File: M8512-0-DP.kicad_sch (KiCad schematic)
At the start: 1 part, among them J1 KL10_6-bay_backplane_connector

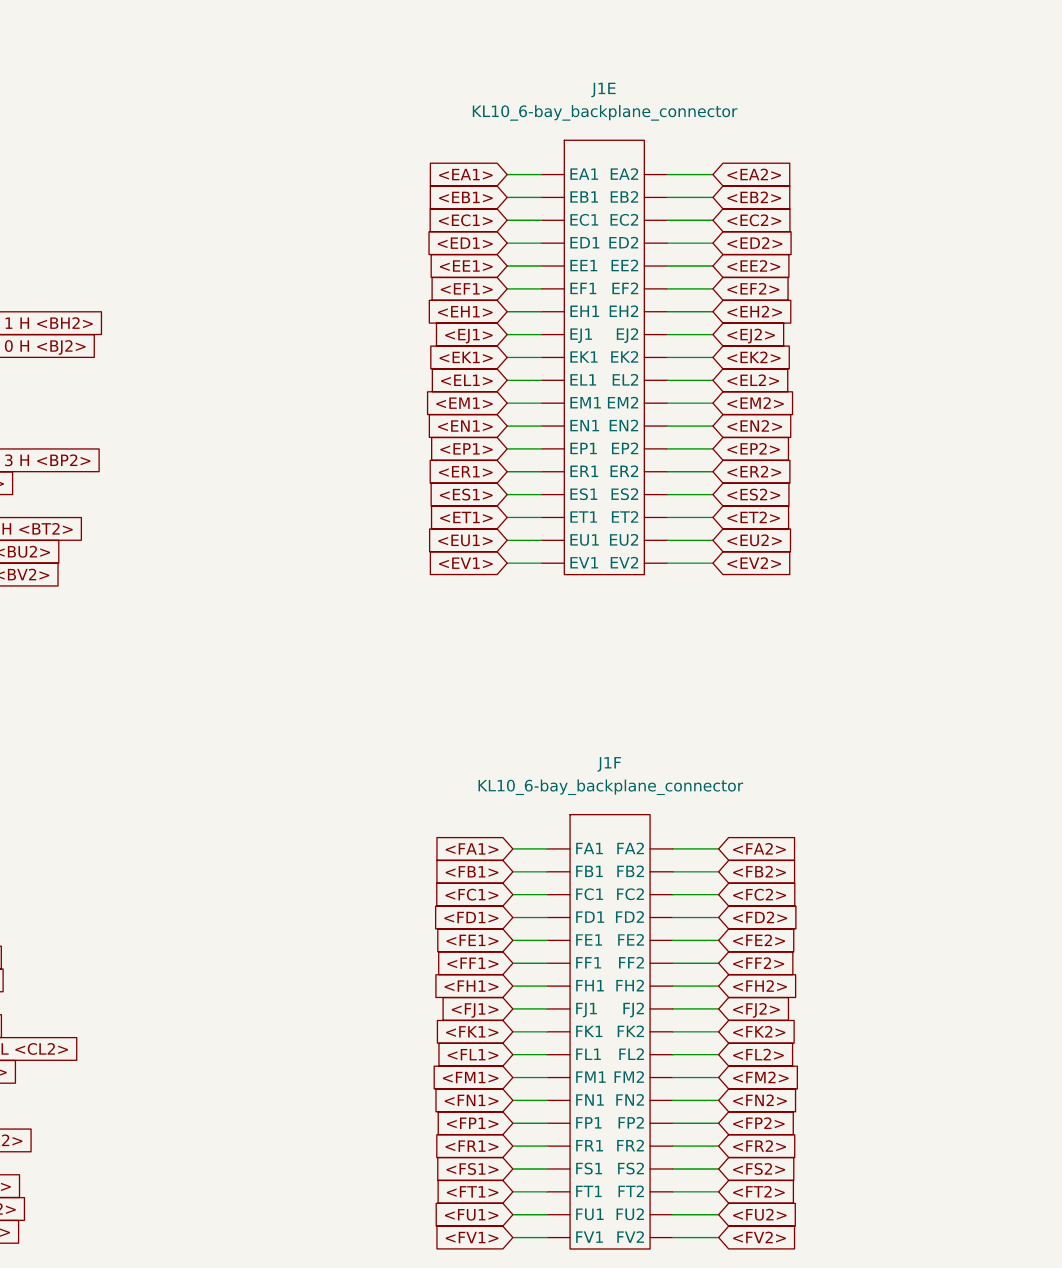
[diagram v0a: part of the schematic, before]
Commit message: Label BP connectors in EDP with their signal names.
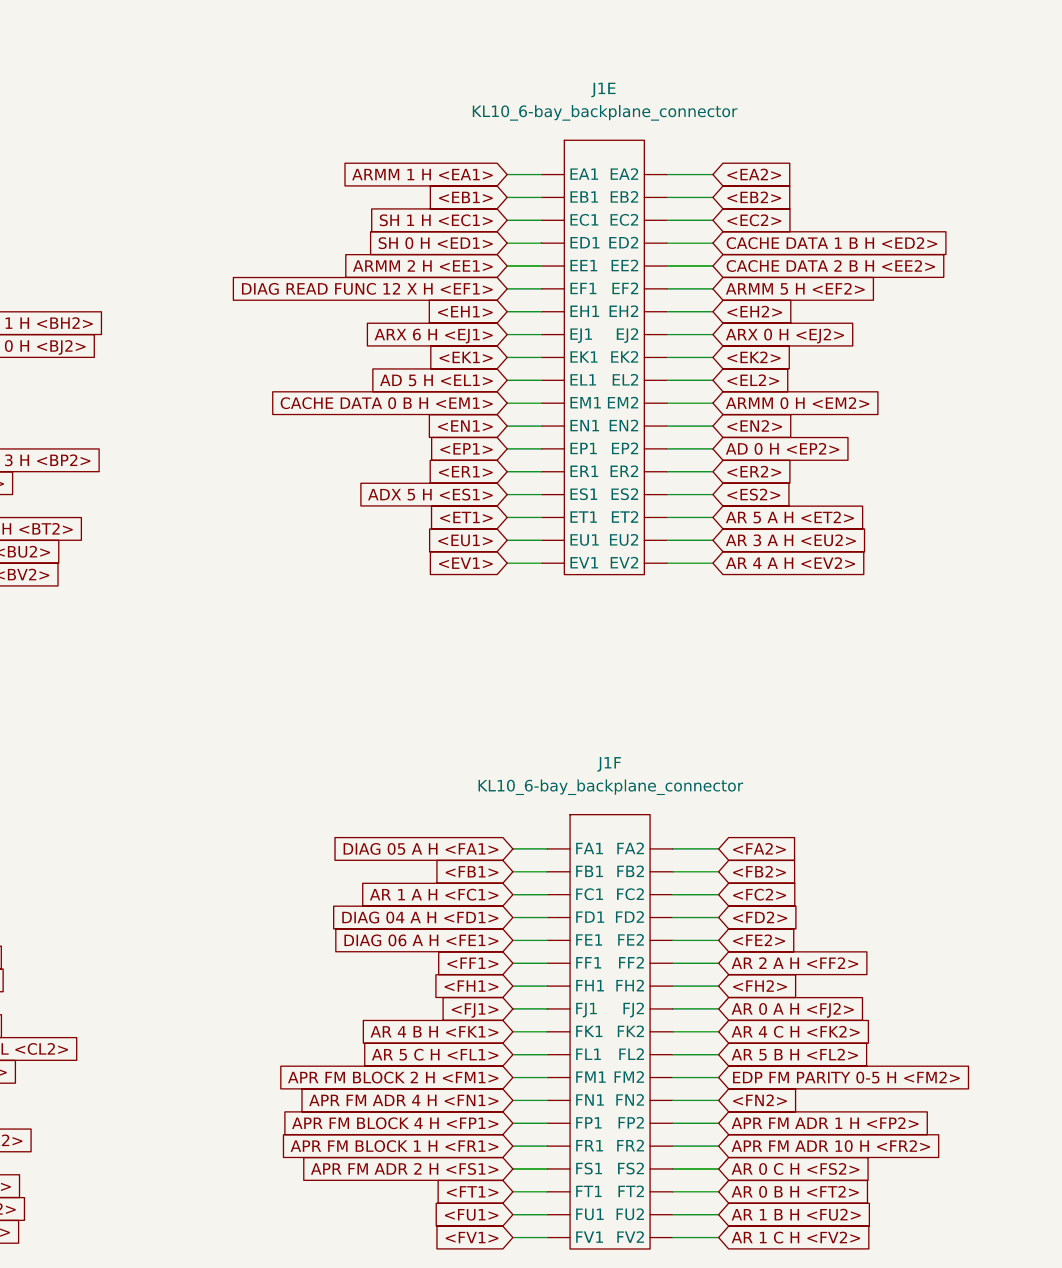
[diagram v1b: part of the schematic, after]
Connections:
- net <EA1> renamed ARMM 1 H <EA1>
- net <EC1> renamed SH 1 H <EC1>
- net <ED1> renamed SH 0 H <ED1>
- net <ED2> renamed CACHE DATA 1 B H <ED2>
- net <EE1> renamed ARMM 2 H <EE1>
- net <EE2> renamed CACHE DATA 2 B H <EE2>
- net <EF1> renamed DIAG READ FUNC 12 X H <EF1>
- net <EF2> renamed ARMM 5 H <EF2>
- net <EJ1> renamed ARX 6 H <EJ1>
- net <EJ2> renamed ARX 0 H <EJ2>
- net <EL1> renamed AD 5 H <EL1>
- net <EM1> renamed CACHE DATA 0 B H <EM1>
- net <EM2> renamed ARMM 0 H <EM2>
- net <EP2> renamed AD 0 H <EP2>
- net <ES1> renamed ADX 5 H <ES1>
- net <ET2> renamed AR 5 A H <ET2>
- net <EU2> renamed AR 3 A H <EU2>
- net <EV2> renamed AR 4 A H <EV2>
- net <FA1> renamed DIAG 05 A H <FA1>
- net <FC1> renamed AR 1 A H <FC1>
- net <FD1> renamed DIAG 04 A H <FD1>
- net <FE1> renamed DIAG 06 A H <FE1>
- net <FF2> renamed AR 2 A H <FF2>
- net <FJ2> renamed AR 0 A H <FJ2>
- net <FK1> renamed AR 4 B H <FK1>
- net <FK2> renamed AR 4 C H <FK2>
- net <FL1> renamed AR 5 C H <FL1>
- net <FL2> renamed AR 5 B H <FL2>
- net <FM1> renamed APR FM BLOCK 2 H <FM1>
- net <FM2> renamed EDP FM PARITY 0-5 H <FM2>
- net <FN1> renamed APR FM ADR 4 H <FN1>
- net <FP1> renamed APR FM BLOCK 4 H <FP1>
- net <FP2> renamed APR FM ADR 1 H <FP2>
- net <FR1> renamed APR FM BLOCK 1 H <FR1>
- net <FR2> renamed APR FM ADR 10 H <FR2>
- net <FS1> renamed APR FM ADR 2 H <FS1>
- net <FS2> renamed AR 0 C H <FS2>
- net <FT2> renamed AR 0 B H <FT2>
- net <FU2> renamed AR 1 B H <FU2>
- net <FV2> renamed AR 1 C H <FV2>

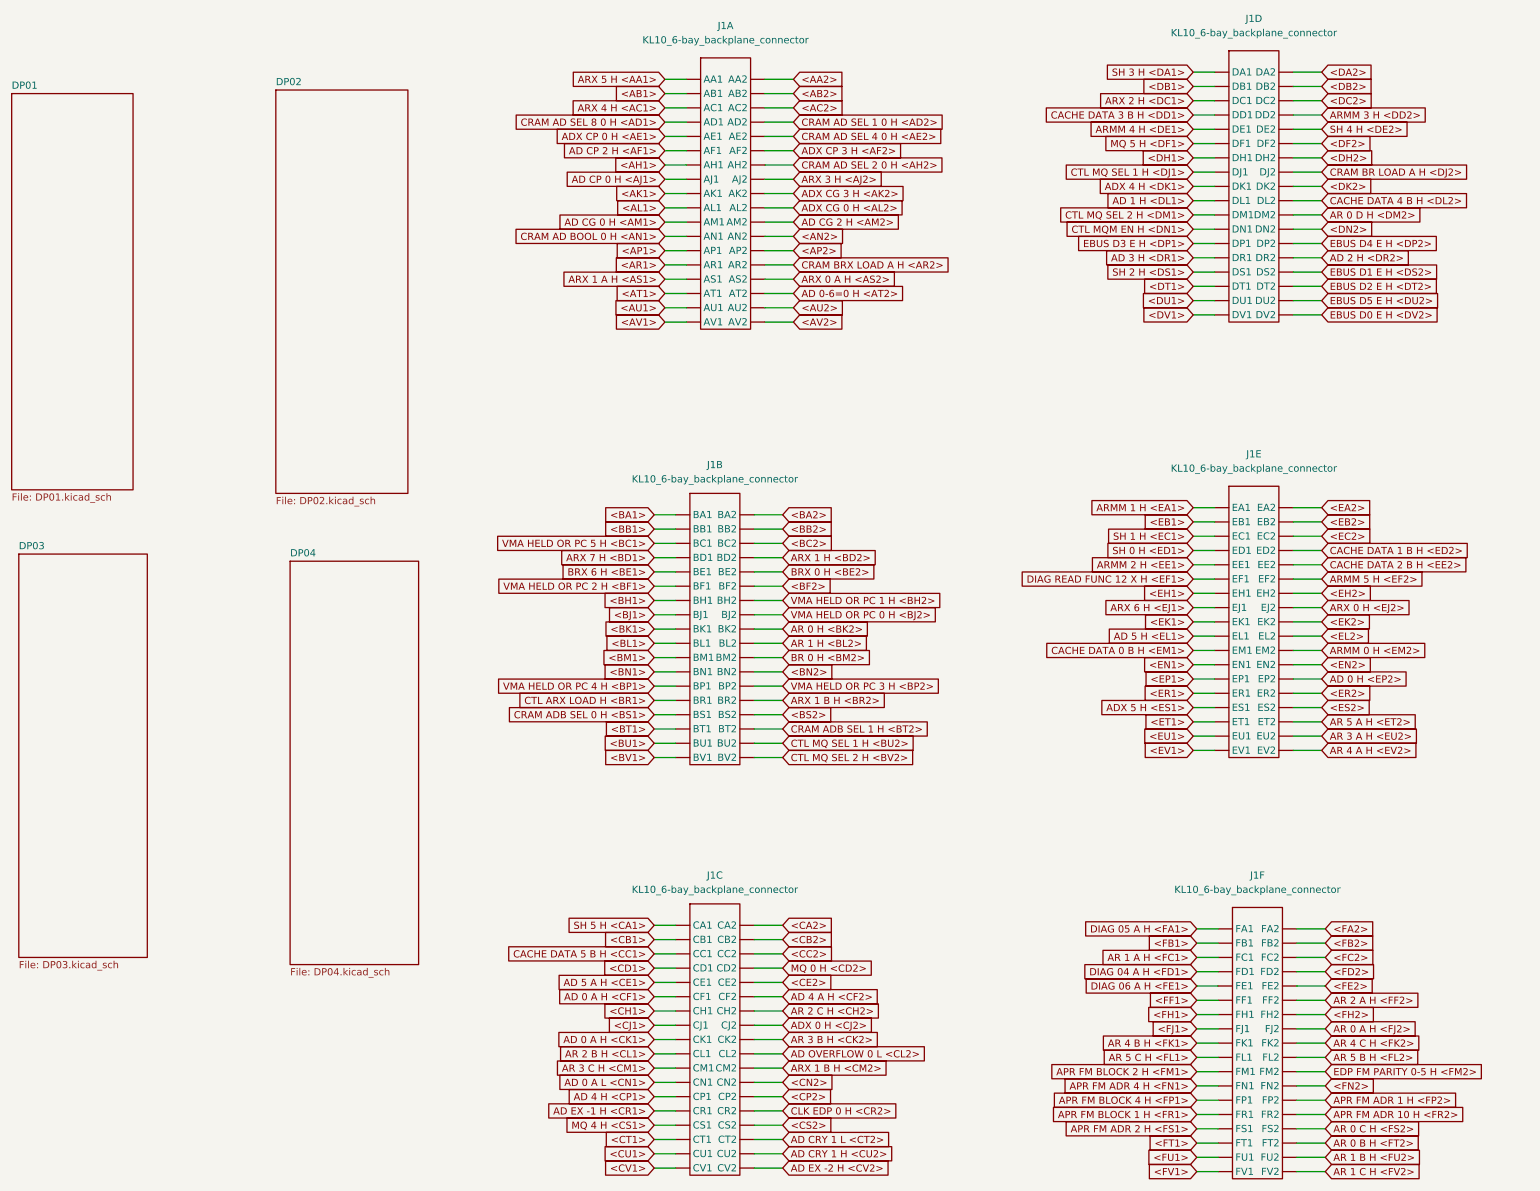
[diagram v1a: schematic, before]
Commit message: Wire up backplane connector GND ECL, V-2.0, V-5.2 and NC and GND ECL tied pins.
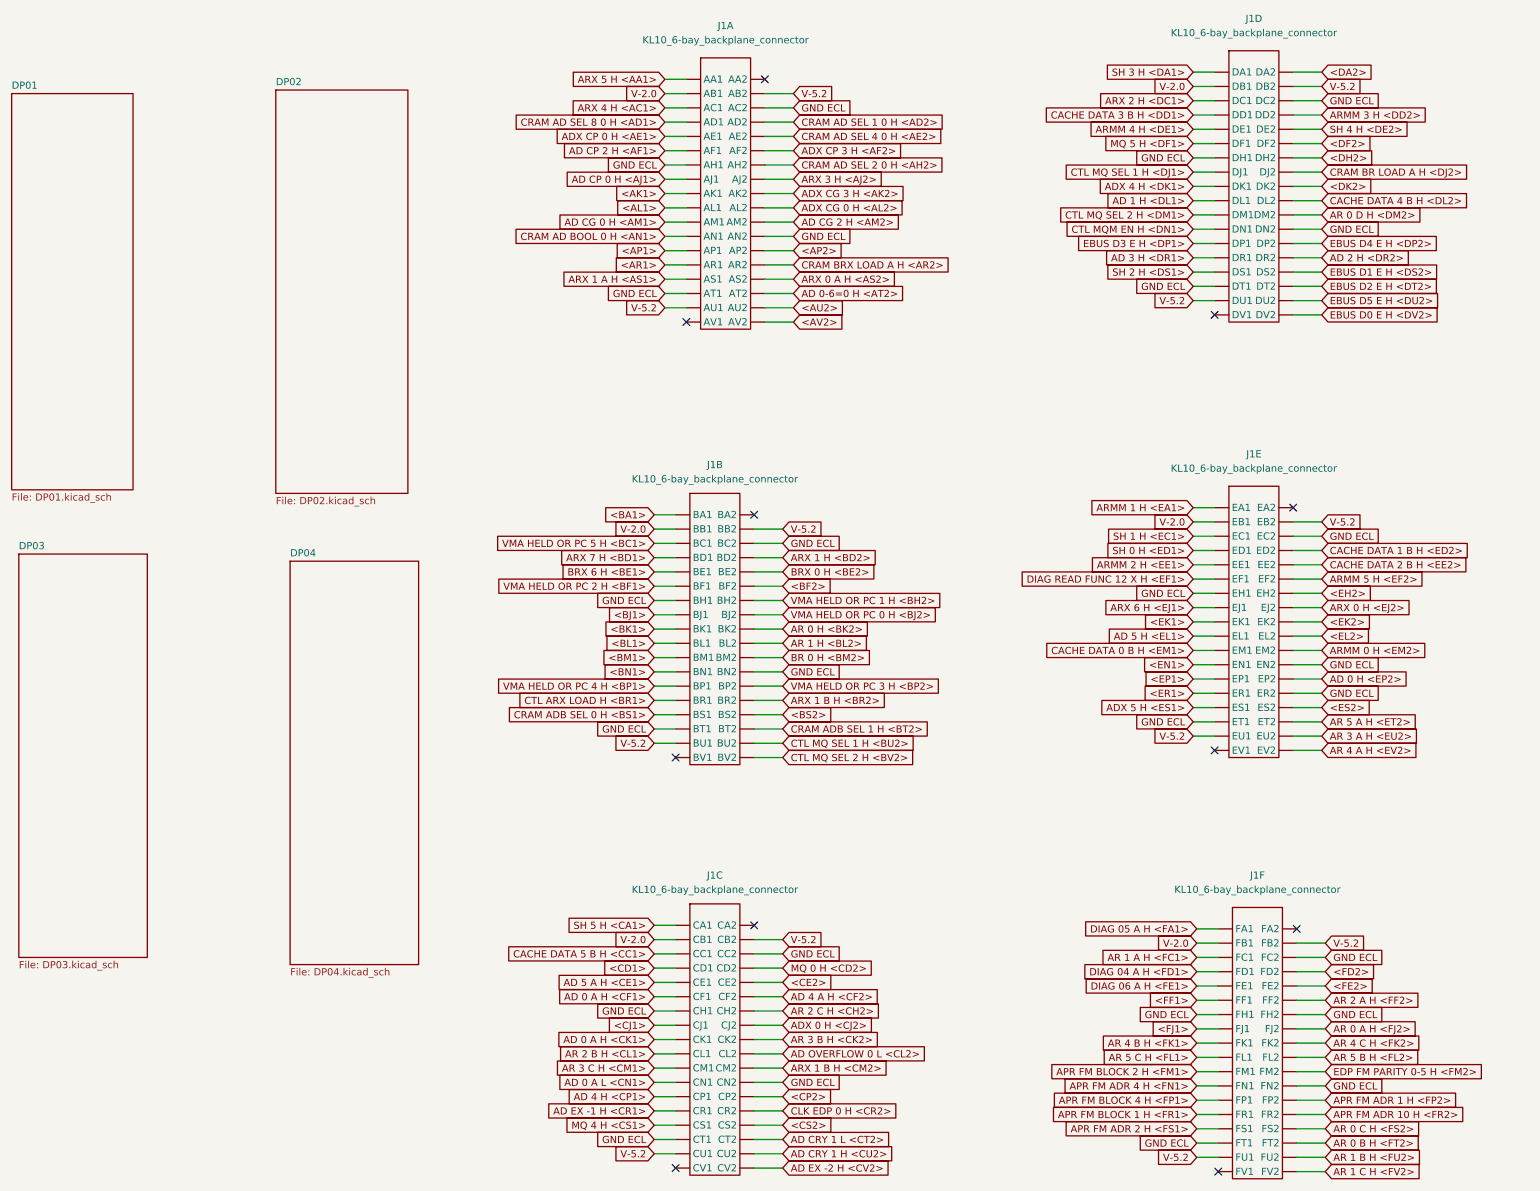
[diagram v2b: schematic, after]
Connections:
- net <AH1> is gone; now on net GND ECL: J1.13 (AH1)
- net <AN2> is gone; now on net GND ECL: J1.24 (AN2)
- net <AT1> is gone; now on net GND ECL: J1.31 (AT1)
- net <AU1> is gone; now on net V-5.2: J1.33 (AU1)
- net <BB1> is gone; now on net V-2.0: J1.39 (BB1)
- net <BB2> is gone; now on net V-5.2: J1.40 (BB2)
- net <BC2> is gone; now on net GND ECL: J1.42 (BC2)
- net <BH1> is gone; now on net GND ECL: J1.49 (BH1)
- net <BN2> is gone; now on net GND ECL: J1.60 (BN2)
- net <BT1> is gone; now on net GND ECL: J1.67 (BT1)
- net <BU1> is gone; now on net V-5.2: J1.69 (BU1)
- net <CB1> is gone; now on net V-2.0: J1.75 (CB1)
- net <CB2> is gone; now on net V-5.2: J1.76 (CB2)
- net <CC2> is gone; now on net GND ECL: J1.78 (CC2)
- net <CH1> is gone; now on net GND ECL: J1.85 (CH1)
- net <CN2> is gone; now on net GND ECL: J1.96 (CN2)
- net <CT1> is gone; now on net GND ECL: J1.103 (CT1)
- net <CU1> is gone; now on net V-5.2: J1.105 (CU1)
- net <DB1> is gone; now on net V-2.0: J1.111 (DB1)
- net <DB2> is gone; now on net V-5.2: J1.112 (DB2)
- net <DC2> is gone; now on net GND ECL: J1.114 (DC2)
- net <DH1> is gone; now on net GND ECL: J1.121 (DH1)
- net <DN2> is gone; now on net GND ECL: J1.132 (DN2)
- net <DT1> is gone; now on net GND ECL: J1.139 (DT1)
- net <DU1> is gone; now on net V-5.2: J1.141 (DU1)
- net <EB1> is gone; now on net V-2.0: J1.147 (EB1)
- net <EB2> is gone; now on net V-5.2: J1.148 (EB2)
- net <EC2> is gone; now on net GND ECL: J1.150 (EC2)
- net <EH1> is gone; now on net GND ECL: J1.157 (EH1)
- net <EN2> is gone; now on net GND ECL: J1.168 (EN2)
- net <ER2> is gone; now on net GND ECL: J1.172 (ER2)
- net <ET1> is gone; now on net GND ECL: J1.175 (ET1)
- net <EU1> is gone; now on net V-5.2: J1.177 (EU1)
- net <FB1> is gone; now on net V-2.0: J1.183 (FB1)
- net <FB2> is gone; now on net V-5.2: J1.184 (FB2)
- net <FC2> is gone; now on net GND ECL: J1.186 (FC2)
- net <FH1> is gone; now on net GND ECL: J1.193 (FH1)
- net <FH2> is gone; now on net GND ECL: J1.194 (FH2)
- net <FN2> is gone; now on net GND ECL: J1.204 (FN2)
- net <FT1> is gone; now on net GND ECL: J1.211 (FT1)
- net <FU1> is gone; now on net V-5.2: J1.213 (FU1)
- net <AA2>: no longer names the net of J1.2 (AA2)
- net <AB1> renamed V-2.0
- net <AB2> renamed V-5.2
- net <AC2> renamed GND ECL
- net <AV1>: no longer names the net of J1.35 (AV1)
- net <BA2>: no longer names the net of J1.38 (BA2)
- net <BV1>: no longer names the net of J1.71 (BV1)
- net <CA2>: no longer names the net of J1.74 (CA2)
- net <CV1>: no longer names the net of J1.107 (CV1)
- net <DV1>: no longer names the net of J1.143 (DV1)
- net <EA2>: no longer names the net of J1.146 (EA2)
- net <EV1>: no longer names the net of J1.179 (EV1)
- net <FA2>: no longer names the net of J1.182 (FA2)
- net <FV1>: no longer names the net of J1.215 (FV1)
- no-connect marks 0 -> 11
